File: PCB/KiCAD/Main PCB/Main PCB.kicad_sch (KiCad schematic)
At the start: 23 parts, among them J2 Conn_02x03_Odd_Even, J3 Conn_01x04, J4 Conn_02x03_Odd_Even, J5 Conn_01x08, Q1 BSS138, Q2 BSS138, U1 Teensy4.0, U3 MIC5219-3.3YM5

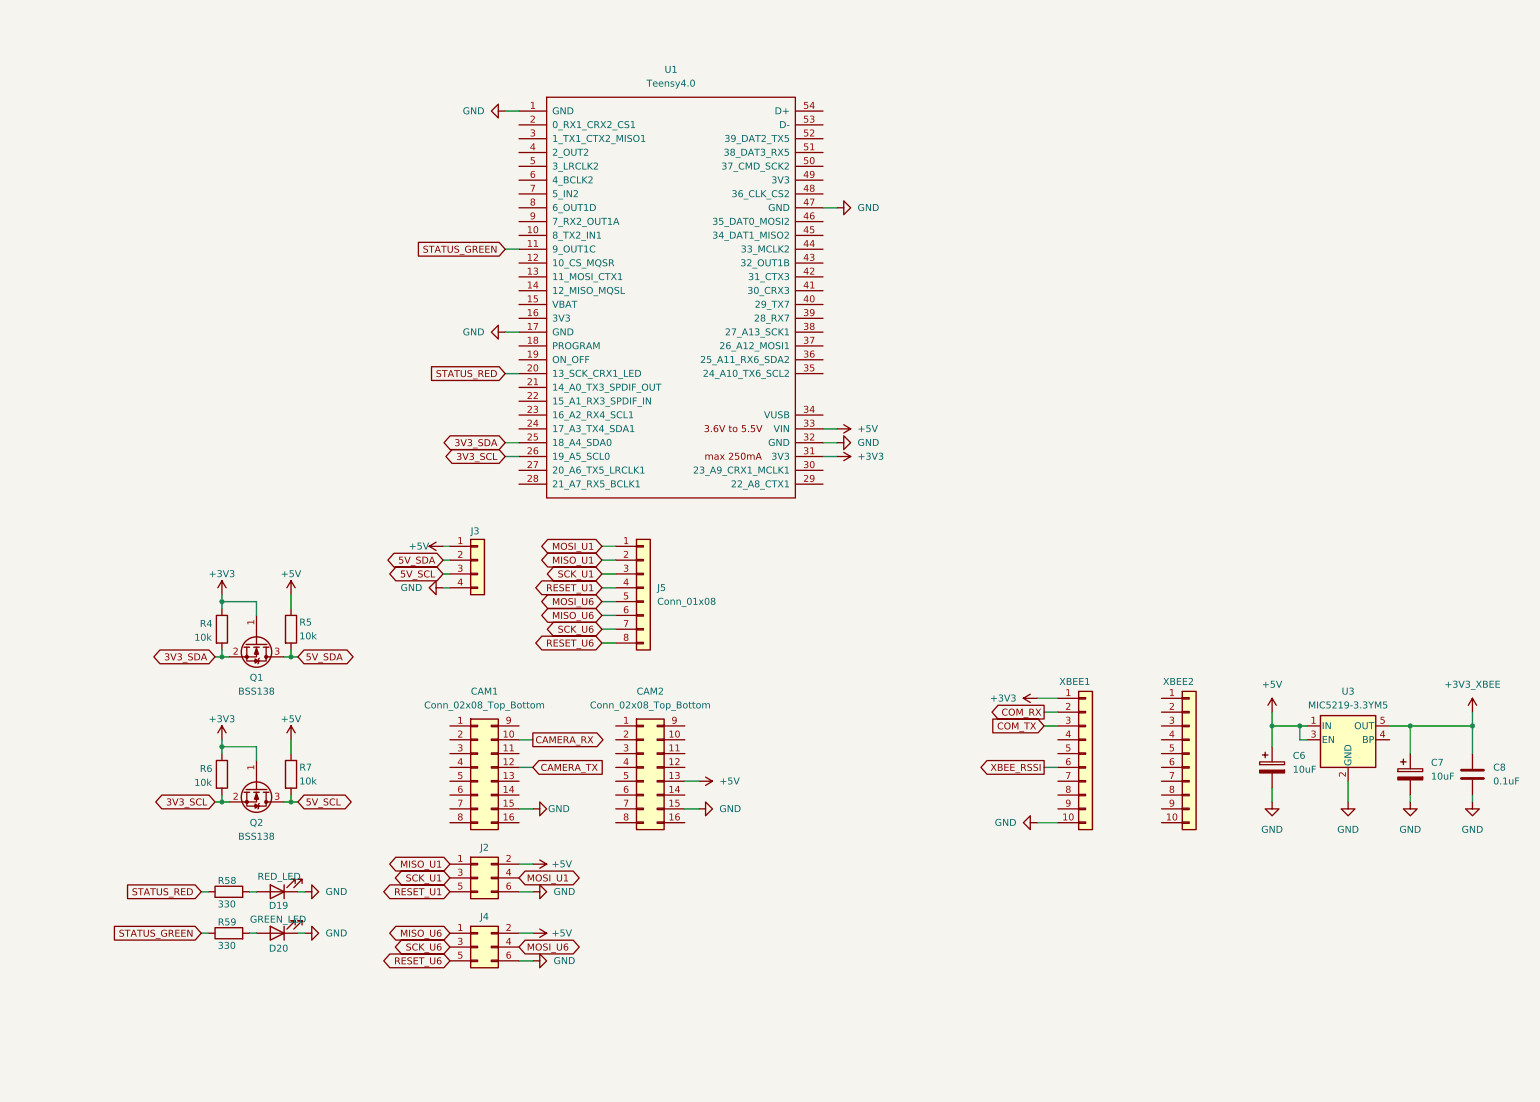
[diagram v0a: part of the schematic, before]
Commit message: More work to the Main PCB and refinement of Via sizes
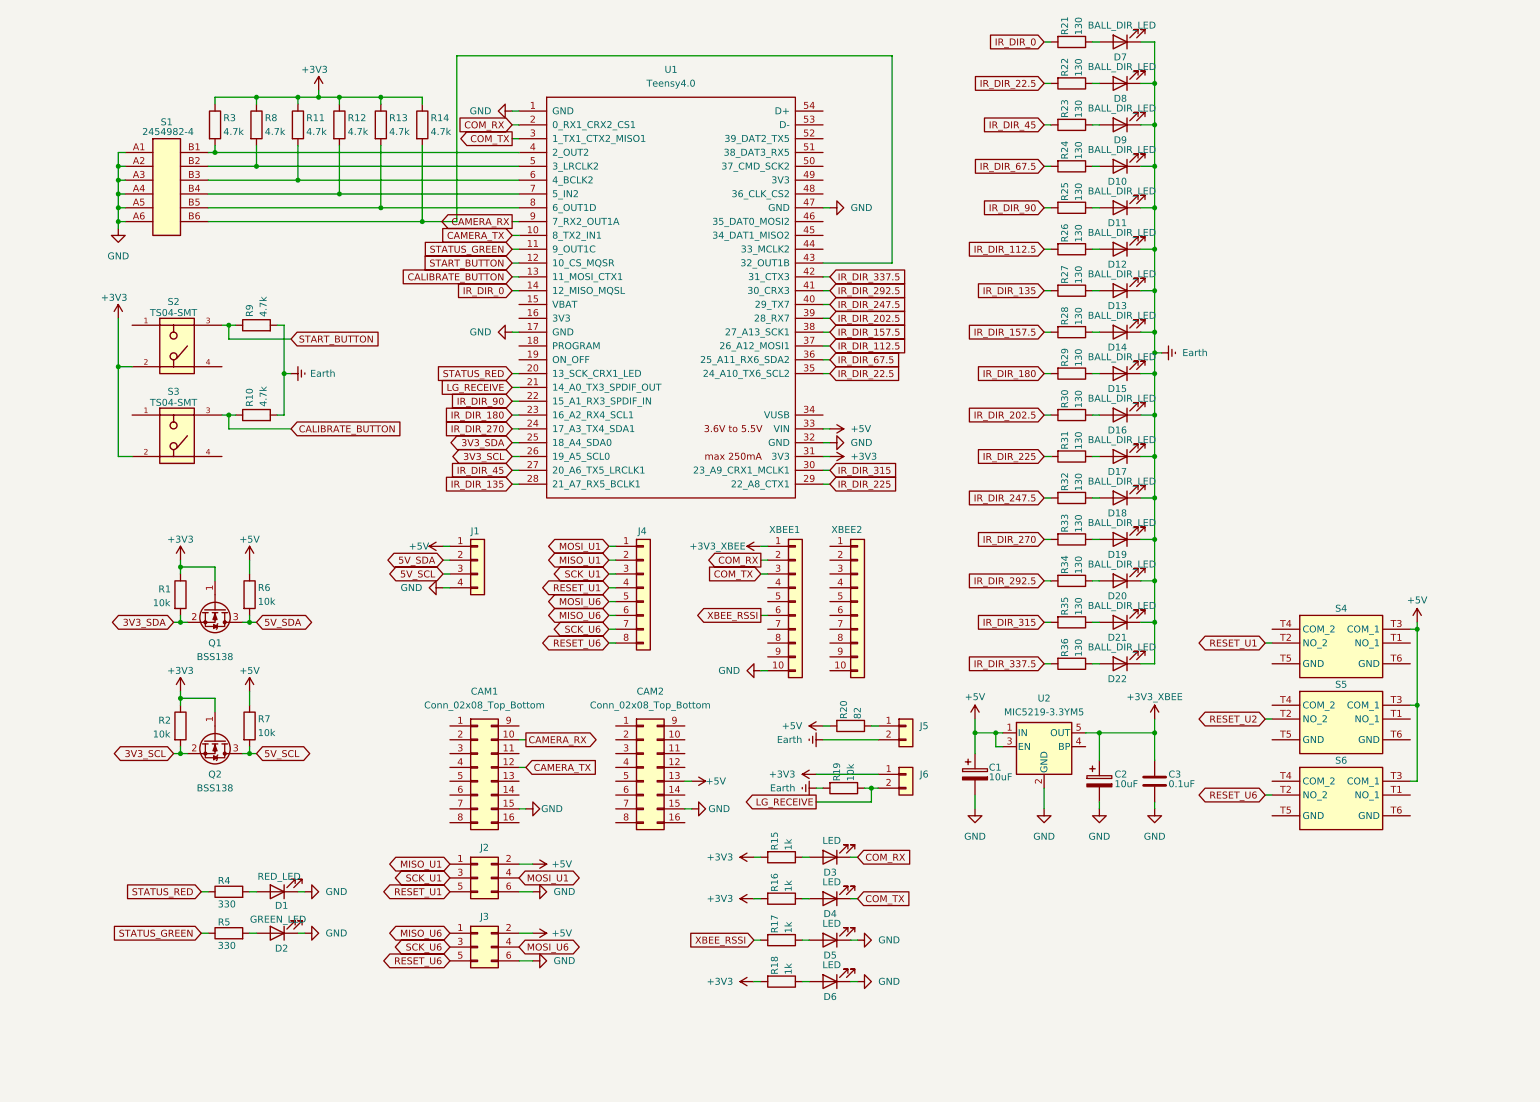
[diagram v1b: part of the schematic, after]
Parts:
- added D10, D11, D12, D13, D14, D15, D16, D17, D18, D19, D20, D21, D22, D7, D8, D9: BALL_DIR_LED, LED_SMD:LED_0805_2012Metric_Pad1.15x1.40mm_HandSolder, symbol Device:LED
- added D3, D4, D5, D6: LED, LED_SMD:LED_0805_2012Metric_Pad1.15x1.40mm_HandSolder, symbol Device:LED
- added J5, J6: Conn_01x02, Connector_JST:JST_PH_B2B-PH-K_1x02_P2.00mm_Vertical, symbol Connector_Generic:Conn_01x02
- added R10, R11, R12, R13, R14, R3, R8, R9: 4.7k, Resistor_SMD:R_0805_2012Metric_Pad1.20x1.40mm_HandSolder, symbol Device:R
- added R15, R16, R17, R18: 1k, Resistor_SMD:R_0805_2012Metric_Pad1.20x1.40mm_HandSolder, symbol Device:R
- added R19: 10k, Resistor_SMD:R_0805_2012Metric_Pad1.20x1.40mm_HandSolder, symbol Device:R
- added R20: 82, Resistor_SMD:R_0805_2012Metric_Pad1.20x1.40mm_HandSolder, symbol Device:R
- added R21, R22, R23, R24, R25, R26, R27, R28, R29, R30, R31, R32, R33, R34, R35, R36: 130, Resistor_SMD:R_0805_2012Metric_Pad1.20x1.40mm_HandSolder, symbol Device:R
- added S1: 2454982-4, DIP_SW_6:DIP_6_SWITCH_THT, symbol DIP_6_SWITCH:2454982-4
- added S2, S3: TS04-SMT, TS04:SW_TS04-66-70-BK-260-SMT, symbol TS04-66-70-BK-260-SMT:TS04-66-70-BK-260-SMT
- added S4, S5, S6: MSLPT5252BG4MTR, MSLPT5252BG4MTR:MSLPT5252BG4MTR, symbol MSLPT5252BG4MTR:MSLPT5252BG4MTR
- renumbered C6 to C1, C7 to C2, C8 to C3, D19 to D1, D20 to D2, J3 to J1, J4 to J3, J5 to J4, R4 to R1, R6 to R2, R58 to R4, R59 to R5, R5 to R6, U3 to U2
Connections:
- net +3V3: now also J6.1 (Pin_1), R11.1, R12.1, R13.1, R14.1, R15.2, R16.2, R18.2, R3.1, R8.1, S2.2, S3.2; no longer XBEE1.1 (Pin_1)
- net +3V3_XBEE: now also XBEE1.1 (Pin_1)
- net +5V: now also R20.2, S4.T3 (COM_1), S5.T3 (COM_1), S6.T3 (COM_1)
- net CAMERA_RX: now also U1.9 (7_RX2_OUT1A)
- net CAMERA_TX: now also U1.10 (8_TX2_IN1)
- net COM_RX: now also U1.2 (0_RX1_CRX2_CS1), D3.1 (K)
- net COM_TX: now also U1.3 (1_TX1_CTX2_MISO1), D4.1 (K)
- net GND: now also D5.1 (K), D6.1 (K), S1.A1, S1.A2, S1.A3, S1.A4, S1.A5, S1.A6
- net RESET_U1: now also S4.T2 (NO_2)
- net RESET_U6: now also S6.T2 (NO_2)
- net XBEE_RSSI: now also R17.2
- net START_BUTTON: now reaches U1.12 (10_CS_MQSR)
- net START_BUTTON: now also R9.1, S2.3
- net CALIBRATE_BUTTON: now reaches U1.13 (11_MOSI_CTX1)
- net CALIBRATE_BUTTON: now also R10.1, S3.3
- net IR_DIR_0: now reaches U1.14 (12_MISO_MQSL)
- net IR_DIR_0: now also R21.2
- net LG_RECEIVE: now reaches U1.21 (14_A0_TX3_SPDIF_OUT)
- net LG_RECEIVE: now also J6.2 (Pin_2), R19.1
- net IR_DIR_90: now reaches U1.22 (15_A1_RX3_SPDIF_IN)
- net IR_DIR_90: now also R25.2
- net IR_DIR_180: now reaches U1.23 (16_A2_RX4_SCL1)
- net IR_DIR_180: now also R29.2
- net IR_DIR_270: now reaches U1.24 (17_A3_TX4_SDA1)
- net IR_DIR_270: now also R33.2
- net IR_DIR_45: now reaches U1.27 (20_A6_TX5_LRCLK1)
- net IR_DIR_45: now also R23.2
- net IR_DIR_135: now reaches U1.28 (21_A7_RX5_BCLK1)
- net IR_DIR_135: now also R27.2
- net IR_DIR_225: now reaches U1.29 (22_A8_CTX1)
- net IR_DIR_225: now also R31.2
- net IR_DIR_315: now reaches U1.30 (23_A9_CRX1_MCLK1)
- net IR_DIR_315: now also R35.2
- net IR_DIR_22.5: now reaches U1.35 (24_A10_TX6_SCL2)
- net IR_DIR_22.5: now also R22.2
- net IR_DIR_67.5: now reaches U1.36 (25_A11_RX6_SDA2)
- net IR_DIR_67.5: now also R24.2
- net IR_DIR_112.5: now reaches U1.37 (26_A12_MOSI1)
- net IR_DIR_112.5: now also R26.2
- net IR_DIR_157.5: now reaches U1.38 (27_A13_SCK1)
- net IR_DIR_157.5: now also R28.2
- net IR_DIR_202.5: now reaches U1.39 (28_RX7)
- net IR_DIR_202.5: now also R30.2
- net at U1.4 (2_OUT2): now also R3.2, S1.B1
- net IR_DIR_247.5: now reaches U1.40 (29_TX7)
- net IR_DIR_247.5: now also R32.2
- net IR_DIR_292.5: now reaches U1.41 (30_CRX3)
- net IR_DIR_292.5: now also R34.2
- net IR_DIR_337.5: now reaches U1.42 (31_CTX3)
- net IR_DIR_337.5: now also R36.2
- net at U1.43 (32_OUT1B): now also R14.2, S1.B6
- net at U1.5 (3_LRCLK2): now also R8.2, S1.B2
- net at U1.6 (4_BCLK2): now also R11.2, S1.B3
- net at U1.7 (5_IN2): now also R12.2, S1.B4
- net at U1.8 (6_OUT1D): now also R13.2, S1.B5
- new net: D9.2 (A), R23.1
- new net: D20.2 (A), R34.1
- new net: D4.2 (A), R16.1
- new net: D18.2 (A), R32.1
- new net: D10.2 (A), R24.1
- new net: D3.2 (A), R15.1
- new net: D14.2 (A), R28.1
- new net: D19.2 (A), R33.1
- new net: D12.2 (A), R26.1
- new net: D15.2 (A), R29.1
- new net: D11.2 (A), R25.1
- new net: D7.2 (A), R21.1
- new net: D21.2 (A), R35.1
- new net: D22.2 (A), R36.1
- new net: D16.2 (A), R30.1
- new net: J5.1 (Pin_1), R20.1
- new net: D17.2 (A), R31.1
- new net: D6.2 (A), R18.1
- new net: D8.2 (A), R22.1
- new net: D13.2 (A), R27.1
- new net: D5.2 (A), R17.1
- new net Earth: D10.1 (K), D11.1 (K), D12.1 (K), D13.1 (K), D14.1 (K), D15.1 (K), D16.1 (K), D17.1 (K), D18.1 (K), D19.1 (K), D20.1 (K), D21.1 (K), D22.1 (K), D7.1 (K), D8.1 (K), D9.1 (K), J5.2 (Pin_2), R10.2, R19.2, R9.2
- new net RESET_U2: S5.T2 (NO_2)
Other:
- moved on the sheet: C1, C2, C3, Q1, Q2, R1, R2, R6, R7, U2, XBEE1, XBEE2

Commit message: Changes to the main PCB
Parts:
- removed D1: RED_LED, LED_SMD:LED_0805_2012Metric_Pad1.15x1.40mm_HandSolder, symbol Device:LED
- removed D10, D11, D12, D13, D14, D15, D16, D17, D18, D19, D20, D21, D22, D7, D8, D9: BALL_DIR_LED, LED_SMD:LED_0805_2012Metric_Pad1.15x1.40mm_HandSolder, symbol Device:LED
- removed D2: GREEN_LED, LED_SMD:LED_0805_2012Metric_Pad1.15x1.40mm_HandSolder, symbol Device:LED
- removed D3, D4, D5, D6: LED, LED_SMD:LED_0805_2012Metric_Pad1.15x1.40mm_HandSolder, symbol Device:LED
- removed J1: Conn_01x04, Connector_JST:JST_PH_B4B-PH-K_1x04_P2.00mm_Vertical, symbol Connector_Generic:Conn_01x04
- removed J2, J3: Conn_02x03_Odd_Even, Connector_IDC:IDC-Header_2x03_P2.54mm_Vertical_SMD, symbol Connector_Generic:Conn_02x03_Odd_Even
- removed J4: Conn_01x08, Connector_JST:JST_PH_B8B-PH-K_1x08_P2.00mm_Vertical, symbol Connector_Generic:Conn_01x08
- removed R15, R16, R17, R18: 1k, Resistor_SMD:R_0805_2012Metric_Pad1.20x1.40mm_HandSolder, symbol Device:R
- removed R21, R22, R23, R24, R25, R26, R27, R28, R29, R30, R31, R32, R33, R34, R35, R36: 130, Resistor_SMD:R_0805_2012Metric_Pad1.20x1.40mm_HandSolder, symbol Device:R
- removed R4, R5: 330, Resistor_SMD:R_0805_2012Metric_Pad1.20x1.40mm_HandSolder, symbol Device:R
- removed S4, S5, S6: MSLPT5252BG4MTR, MSLPT5252BG4MTR:MSLPT5252BG4MTR, symbol MSLPT5252BG4MTR:MSLPT5252BG4MTR
- removed XBEE1, XBEE2: Conn_01x10, Connector_PinSocket_2.00mm:PinSocket_1x10_P2.00mm_Vertical, symbol Connector_Generic:Conn_01x10
- added F1: Fuse, Fuse:Fuseholder_Blade_Mini_Keystone_3568, symbol Device:Fuse
- added J1: Conn_01x02, Connector_AMASS:AMASS_XT60-M_1x02_P7.20mm_Vertical, symbol Connector_Generic:Conn_01x02
- added J5: Conn_01x02, Connector_JST:JST_PH_B2B-PH-K_1x02_P2.00mm_Vertical, symbol Connector_Generic:Conn_01x02
- added J6, J7: Conn_01x04, Connector_JST:JST_PH_B4B-PH-K_1x04_P2.00mm_Vertical, symbol Connector_Generic:Conn_01x04
- added S2: 1101M2S3CGE2, 1101M2S3CGE2:1101M2S3CGE2, symbol 1101M2S3CGE2:1101M2S3CGE2
- added U1: ~, Pololu:D36V28F5, symbol Pololu:D36V28F5
- added U2: Teensy4.1, Teensy:Teensy41, symbol teensy:Teensy4.1
- renumbered C1 to C24, C2 to C25, C3 to C26, J5 to J2, J6 to J3, Q2 to Q1, Q1 to Q2, R3 to R1, R20 to R10, R2 to R11, R7 to R12, R1 to R13, R6 to R14, R8 to R2, R11 to R3, R12 to R4, R13 to R5, R14 to R6, R9 to R7, R10 to R8, R19 to R9, S2 to S3, S3 to S4, U1 to U3, U2 to U8
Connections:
- net +3V3_XBEE is gone; now on net +3V3: C25.1, C26.1, U8.5 (OUT)
- net Earth is gone; now on net GND: J2.2 (Pin_2), R7.2, R8.2, R9.2
- net +3V3: no longer S3.2, S4.2, U3.31 (3V3)
- net +5V: now also U1.6 (OUT), U2.48 (VIN)
- net 3V3_SCL: now also U2.41 (19_A5_SCL)
- net 3V3_SDA: now also U2.40 (18_A4_SDA)
- net CALIBRATE_BUTTON: now also U2.13 (11_MOSI_CTX1); no longer U3.13 (11_MOSI_CTX1)
- net CAMERA_RX: now also U2.9 (7_RX2_OUT1A); no longer U3.9 (7_RX2_OUT1A)
- net CAMERA_TX: now also U2.10 (8_TX2_IN1); no longer U3.10 (8_TX2_IN1)
- net COM_RX: now also U2.43 (21_A7_RX5_BCLK1); no longer U3.2 (0_RX1_CRX2_CS1)
- net COM_TX: now also U2.42 (20_A6_TX5_LRCLK1); no longer U3.3 (1_TX1_CTX2_MISO1)
- net GND: now also J1.1 (Pin_1), J5.2 (Pin_2), U1.4 (GND_1), U1.5 (GND_2), U2.1 (GND), U2.34 (GND), U2.47 (GND), U2.52 (GND)
- net IR_DIR_0: now also U2.4 (2_OUT2); no longer U3.14 (12_MISO_MQSL)
- net IR_DIR_112.5: now also U2.27 (35_TX8); no longer U3.37 (26_A12_MOSI1)
- net IR_DIR_135: now also U2.36 (14_A0_TX3_SPDIF_OUT); no longer U3.28 (21_A7_RX5_BCLK1)
- net IR_DIR_157.5: now also U2.28 (36_CS); no longer U3.38 (27_A13_SCK1)
- net IR_DIR_180: now also U2.6 (4_BCLK2); no longer U3.23 (16_A2_RX4_SCL1)
- net IR_DIR_202.5: now also U2.29 (37_CS); no longer U3.39 (28_RX7)
- net IR_DIR_22.5: now also U2.25 (33_MCLK2); no longer U3.35 (24_A10_TX6_SCL2)
- net IR_DIR_225: now also U2.37 (15_A1_RX3_SPDIF_IN); no longer U3.29 (22_A8_CTX1)
- net IR_DIR_247.5: now also U2.30 (38_CS1_IN1); no longer U3.40 (29_TX7)
- net IR_DIR_270: now also U2.7 (5_IN2); no longer U3.24 (17_A3_TX4_SDA1)
- net IR_DIR_292.5: now also U2.31 (39_MISO1_OUT1A); no longer U3.41 (30_CRX3)
- net IR_DIR_315: now also U2.38 (16_A2_RX4_SCL1); no longer U3.30 (23_A9_CRX1_MCLK1)
- net IR_DIR_337.5: now also U2.32 (40_A16); no longer U3.42 (31_CTX3)
- net IR_DIR_45: now also U2.14 (12_MISO_MQSL); no longer U3.27 (20_A6_TX5_LRCLK1)
- net IR_DIR_67.5: now also U2.26 (34_RX8); no longer U3.36 (25_A11_RX6_SDA2)
- net IR_DIR_90: now also U2.5 (3_LRCLK2); no longer U3.22 (15_A1_RX3_SPDIF_IN)
- net LG_RECEIVE: now also U3.22 (15_A1_RX3_SPDIF_IN); no longer U3.21 (14_A0_TX3_SPDIF_OUT)
- net START_BUTTON: now also U2.12 (10_CS_MQSR); no longer U3.12 (10_CS_MQSR)
- net at R3.2, S1.B3: now also U2.21 (29_TX7); no longer U3.6 (4_BCLK2)
- net at R4.2, S1.B4: now also U2.22 (30_CRX3); no longer U3.7 (5_IN2)
- net at R2.2, S1.B2: now also U2.20 (28_RX7); no longer U3.5 (3_LRCLK2)
- net at R6.2, S1.B6: now also U2.24 (32_OUT1B); no longer U3.43 (32_OUT1B)
- net at R1.2, S1.B1: now also U2.19 (27_A13_SCK1); no longer U3.4 (2_OUT2)
- net TSSP_2_A2: now reaches U3.44 (33_MCLK2)
- net at R5.2, S1.B5: now also U2.23 (31_CTX3); no longer U3.8 (6_OUT1D)
- net STATUS_GREEN renamed MOTOR_4_DIR
- net STATUS_RED renamed STATUS_RED_4_0
- new net: F1.1, J1.2 (Pin_2)
- new net: F1.2, S2.2 (COM)
- new net +12V: S2.3 (NO), U1.3 (IN)
- new net +3V3_4_0: J5.1 (Pin_1), U3.31 (3V3)
- new net +3V3_4_1: S3.2, S4.2, U2.46 (3V3)
- new net LED_1_A0: J6.2 (Pin_2), U3.13 (11_MOSI_CTX1)
- new net LED_1_A1: J6.3 (Pin_3), U3.14 (12_MISO_MQSL)
- new net LED_1_A2: J6.4 (Pin_4), U3.23 (16_A2_RX4_SCL1)
- new net LED_1_OUT: J6.1 (Pin_1), U3.12 (10_CS_MQSR)
- new net LED_2_A0: J7.2 (Pin_2), U3.27 (20_A6_TX5_LRCLK1)
- new net LED_2_A1: J7.3 (Pin_3), U3.28 (21_A7_RX5_BCLK1)
- new net LED_2_A2: J7.4 (Pin_4), U3.35 (24_A10_TX6_SCL2)
- new net LED_2_OUT: J7.1 (Pin_1), U3.24 (17_A3_TX4_SDA1)
- new net MOTOR_1_DIR: U3.5 (3_LRCLK2)
- new net MOTOR_1_SPEED: U3.4 (2_OUT2)
- new net MOTOR_2_DIR: U3.7 (5_IN2)
- new net MOTOR_2_SPEED: U3.6 (4_BCLK2)
- new net MOTOR_3_DIR: U3.9 (7_RX2_OUT1A)
- new net MOTOR_3_SPEED: U3.8 (6_OUT1D)
- new net MOTOR_4_SPEED: U3.10 (8_TX2_IN1)
- new net STATUS_GREEN_4_0: U3.21 (14_A0_TX3_SPDIF_OUT)
- new net STATUS_GREEN_4_1: U2.11 (9_OUT1C)
- new net STATUS_RED_4_1: U2.35 (13_SCK_LED)
- new net TEENSY_RX: U2.2 (0_RX1_CRX2_CS1), U3.3 (1_TX1_CTX2_MISO1)
- new net TEENSY_TX: U2.3 (1_TX1_CTX2_MISO1), U3.2 (0_RX1_CRX2_CS1)
- new net TSSP_1_A0: U3.39 (28_RX7)
- new net TSSP_1_A1: U3.40 (29_TX7)
- new net TSSP_1_A2: U3.41 (30_CRX3)
- new net TSSP_1_OUT: U3.29 (22_A8_CTX1)
- new net TSSP_2_A0: U3.42 (31_CTX3)
- new net TSSP_2_A1: U3.43 (32_OUT1B)
- new net TSSP_2_OUT: U3.30 (23_A9_CRX1_MCLK1)
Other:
- added sheet Communication (communication.kicad_sch)
- added sheet LED Indicators (led_indicators.kicad_sch)
- added sheet Motors (motors.kicad_sch)
- moved on the sheet: C24, C25, C26, CAM1, CAM2, J2, J3, Q1, Q2, R1, R10, R11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

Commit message: Updated to main PCB
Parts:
- added J8: Conn_01x04, Connector_JST:JST_PH_B4B-PH-K_1x04_P2.00mm_Vertical, symbol Connector_Generic:Conn_01x04
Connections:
- net +3V3_4_0: now also J8.1 (Pin_1)
- net 3V3_SCL: now also J8.3 (Pin_3)
- net 3V3_SDA: now also J8.2 (Pin_2)
- net GND: now also J8.4 (Pin_4)
